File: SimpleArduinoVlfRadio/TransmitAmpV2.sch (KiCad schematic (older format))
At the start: 6 parts

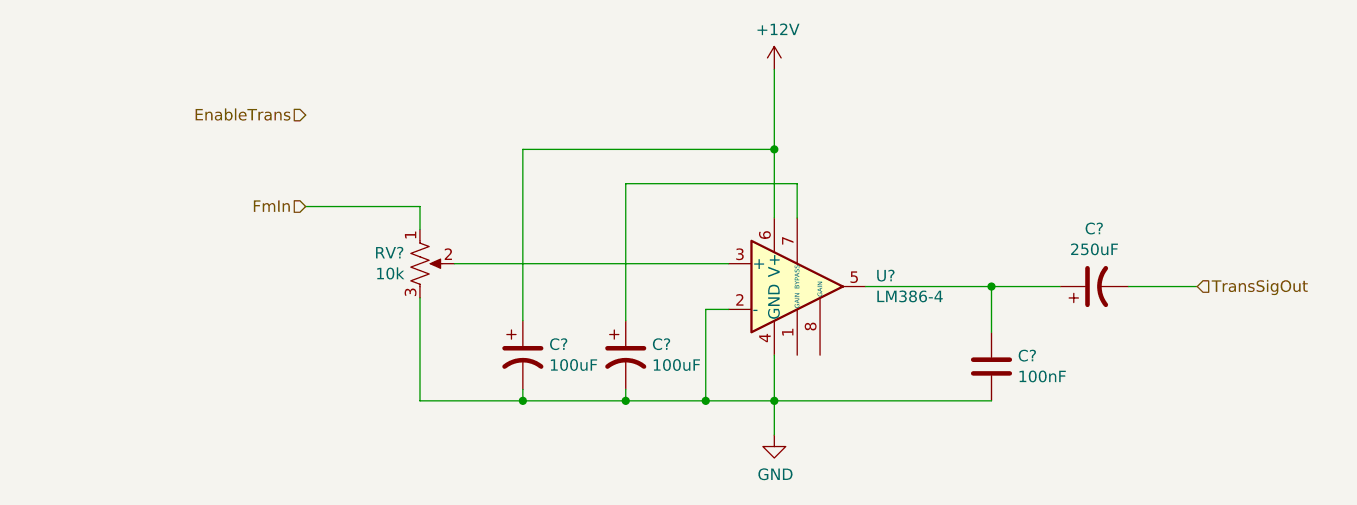
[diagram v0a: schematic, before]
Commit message: Updates to include new transmit amplifier design
Using LM386N-4 instead of LM1875
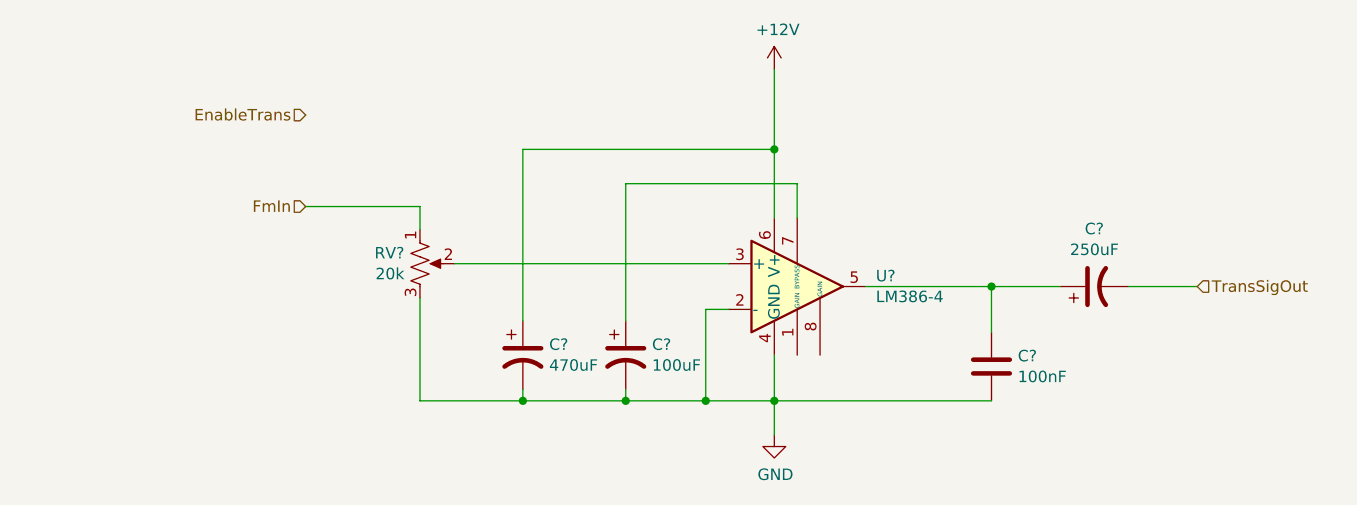
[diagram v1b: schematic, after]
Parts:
- C?: value 100uF -> 470uF
- RV?: value 10k -> 20k
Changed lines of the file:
@@
 P 4600 3750
 F 0 "C?" H 4715 3796 50  0000 L CNN
-F 1 "100uF" H 4715 3705 50  0000 L CNN
+F 1 "470uF" H 4715 3705 50  0000 L CNN
 F 2 "" H 4600 3750 50  0001 C CNN
 F 3 "~" H 4600 3750 50  0001 C CNN
@@
 P 4150 3350
 F 0 "RV?" H 4082 3396 50  0000 R CNN
-F 1 "10k" H 4082 3305 50  0000 R CNN
+F 1 "20k" H 4082 3305 50  0000 R CNN
 F 2 "" H 4150 3350 50  0001 C CNN
 F 3 "~" H 4150 3350 50  0001 C CNN

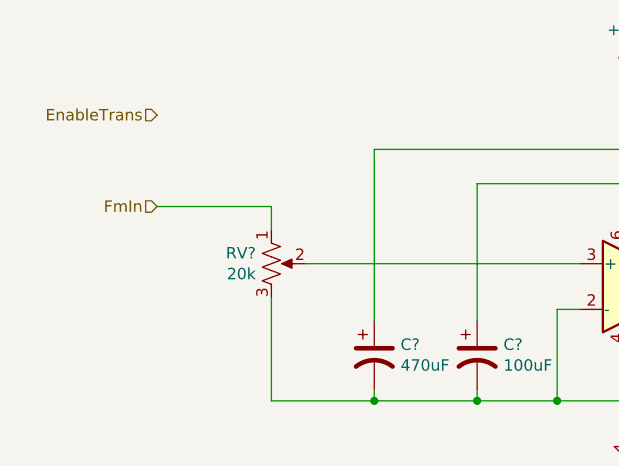
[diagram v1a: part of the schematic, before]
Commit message: Add input capacitor
Filter out DC with an input capacitor.
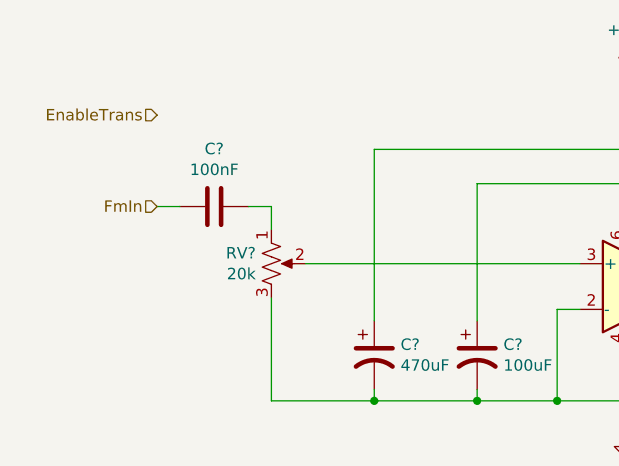
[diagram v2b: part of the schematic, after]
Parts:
- added C?: 100nF, symbol Device:C
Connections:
- net FmIn: now also C?.2; no longer RV?.1
- new net: C?.1, RV?.1
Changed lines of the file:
@@
 Wire Wire Line
 	4150 3200 4150 3100
-Wire Wire Line
-	4150 3100 3650 3100
 Text HLabel 3650 3100 0    50   Input ~ 0
 FmIn
@@
 	5700 2500 5700 2850
 Connection ~ 5700 2850
+$Comp
+L Device:C C?
+U 1 1 61E018D6
+P 3900 3100
+F 0 "C?" V 3648 3100 50  0000 C CNN
+F 1 "100nF" V 3739 3100 50  0000 C CNN
+F 2 "" H 3938 2950 50  0001 C CNN
+F 3 "~" H 3900 3100 50  0001 C CNN
+	1    3900 3100
+	0    1    1    0
+$EndComp
+Wire Wire Line
+	4150 3100 4050 3100
+Wire Wire Line
+	3750 3100 3650 3100
 $EndSCHEMATC

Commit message: Updates to overall layout.
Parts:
- added R?: 100k, symbol Device:R_US
- C?: value 250uF -> 250uF (50V+)
- C?: value 100nF -> 100nF (100V+ Metalized)
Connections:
- net at RV?.1: now also R?.1; no longer C?.1
- new net: C?.1, R?.2
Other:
- moved on the sheet: C?
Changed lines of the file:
@@
 $Descr A4 11693 8268
 encoding utf-8
-Sheet 5 5
+Sheet 4 10
 Title ""
 Date ""
@@
 P 6650 3800
 F 0 "C?" H 6765 3846 50  0000 L CNN
-F 1 "100nF" H 6765 3755 50  0000 L CNN
+F 1 "100nF (100V+ Metalized)" H 6765 3755 50  0000 L CNN
 F 2 "" H 6688 3650 50  0001 C CNN
 F 3 "~" H 6650 3800 50  0001 C CNN
@@
 P 7100 3450
 F 0 "C?" V 7352 3450 50  0000 C CNN
-F 1 "250uF" V 7261 3450 50  0000 C CNN
+F 1 "250uF (50V+)" V 7261 3450 50  0000 C CNN
 F 2 "" H 7100 3450 50  0001 C CNN
 F 3 "~" H 7100 3450 50  0001 C CNN
@@
 	4150 3950 4600 3950
 Connection ~ 4600 3950
-Wire Wire Line
-	4150 3200 4150 3100
-Text HLabel 3650 3100 0    50   Input ~ 0
+Text HLabel 3000 3100 0    50   Input ~ 0
 FmIn
 Text HLabel 7550 3450 2    50   Input ~ 0
 TransSigOut
-Text HLabel 3650 2700 0    50   Input ~ 0
+Text HLabel 3000 2700 0    50   Input ~ 0
 EnableTrans
 Wire Wire Line
@@
 L Device:C C?
 U 1 1 61E018D6
-P 3900 3100
-F 0 "C?" V 3648 3100 50  0000 C CNN
-F 1 "100nF" V 3739 3100 50  0000 C CNN
-F 2 "" H 3938 2950 50  0001 C CNN
-F 3 "~" H 3900 3100 50  0001 C CNN
-	1    3900 3100
+P 3250 3100
+F 0 "C?" V 2998 3100 50  0000 C CNN
+F 1 "100nF" V 3089 3100 50  0000 C CNN
+F 2 "" H 3288 2950 50  0001 C CNN
+F 3 "~" H 3250 3100 50  0001 C CNN
+	1    3250 3100
 	0    1    1    0
 $EndComp
 Wire Wire Line
-	4150 3100 4050 3100
+	3100 3100 3000 3100
+$Comp
+L Device:R_US R?
+U 1 1 61E4A5DB
+P 3750 3100
+F 0 "R?" V 3545 3100 50  0000 C CNN
+F 1 "100k" V 3636 3100 50  0000 C CNN
+F 2 "" V 3790 3090 50  0001 C CNN
+F 3 "~" H 3750 3100 50  0001 C CNN
+	1    3750 3100
+	0    1    1    0
+$EndComp
 Wire Wire Line
-	3750 3100 3650 3100
+	3400 3100 3600 3100
+Wire Wire Line
+	3900 3100 4150 3100
+Wire Wire Line
+	4150 3100 4150 3200
 $EndSCHEMATC

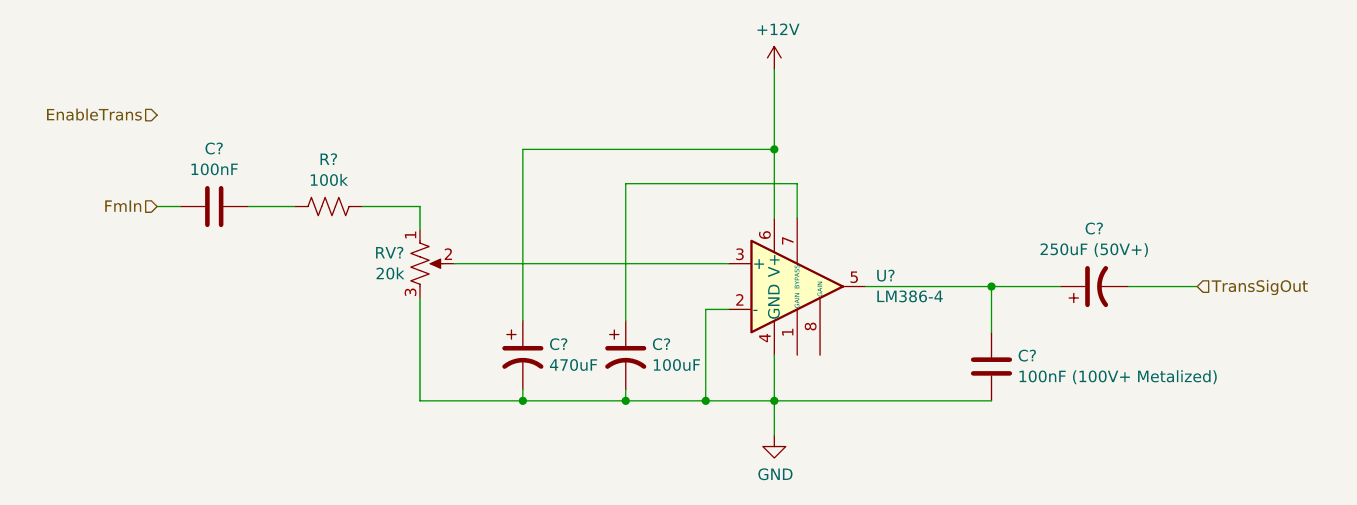
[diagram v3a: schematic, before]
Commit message: Updated Transmitter and finished fsk receiver
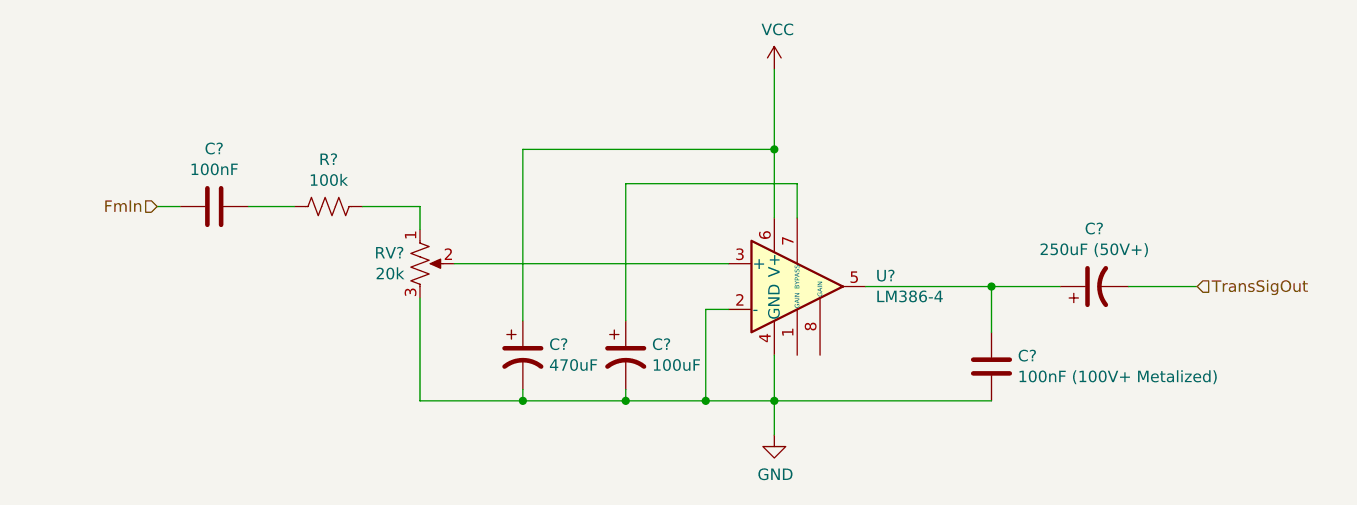
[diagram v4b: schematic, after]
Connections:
- net +12V renamed VCC
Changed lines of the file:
@@
 $Descr A4 11693 8268
 encoding utf-8
-Sheet 4 10
+Sheet 4 14
 Title ""
 Date ""
@@
 $EndDescr
 $Comp
+L power:GND #PWR?
+U 1 1 61DDF91B
+P 5700 4100
+AR Path="/61DDCE18/61DDF91B" Ref="#PWR?"  Part="1"
+AR Path="/62C5E0F5/61DDF91B" Ref="#PWR?"  Part="1"
+F 0 "#PWR?" H 5700 3850 50  0001 C CNN
+F 1 "GND" H 5705 3927 50  0000 C CNN
+F 2 "" H 5700 4100 50  0001 C CNN
+F 3 "" H 5700 4100 50  0001 C CNN
+	1    5700 4100
+	1    0    0    -1
+$EndComp
+Wire Wire Line
+	5500 3550 5400 3550
+Wire Wire Line
+	5400 3550 5400 3950
+Wire Wire Line
+	5400 3950 5700 3950
+Wire Wire Line
+	5700 3950 5700 4100
+Wire Wire Line
+	5700 3750 5700 3950
+Connection ~ 5700 3950
+Wire Wire Line
+	6100 3450 6650 3450
+Wire Wire Line
+	5800 3150 5800 3000
+Wire Wire Line
+	5050 3900 5050 3950
+Wire Wire Line
+	5050 3950 5400 3950
+Connection ~ 5400 3950
+$Comp
+L Device:C C?
+U 1 1 61DE66BC
+P 6650 3800
+AR Path="/61DDCE18/61DE66BC" Ref="C?"  Part="1"
+AR Path="/62C5E0F5/61DE66BC" Ref="C?"  Part="1"
+F 0 "C?" H 6765 3846 50  0000 L CNN
+F 1 "100nF (100V+ Metalized)" H 6765 3755 50  0000 L CNN
+F 2 "" H 6688 3650 50  0001 C CNN
+F 3 "~" H 6650 3800 50  0001 C CNN
+	1    6650 3800
+	1    0    0    -1
+$EndComp
+Wire Wire Line
+	6650 3650 6650 3450
+Connection ~ 6650 3450
+Wire Wire Line
+	6650 3450 6950 3450
+Wire Wire Line
+	6650 3950 5700 3950
+$Comp
+L Device:CP1 C?
+U 1 1 61DE1BB3
+P 5050 3750
+AR Path="/61DDCE18/61DE1BB3" Ref="C?"  Part="1"
+AR Path="/62C5E0F5/61DE1BB3" Ref="C?"  Part="1"
+F 0 "C?" H 5165 3796 50  0000 L CNN
+F 1 "100uF" H 5165 3705 50  0000 L CNN
+F 2 "" H 5050 3750 50  0001 C CNN
+F 3 "~" H 5050 3750 50  0001 C CNN
+	1    5050 3750
+	1    0    0    -1
+$EndComp
+$Comp
+L Device:CP1 C?
+U 1 1 61DE52DF
+P 7100 3450
+AR Path="/61DDCE18/61DE52DF" Ref="C?"  Part="1"
+AR Path="/62C5E0F5/61DE52DF" Ref="C?"  Part="1"
+F 0 "C?" V 7352 3450 50  0000 C CNN
+F 1 "250uF (50V+)" V 7261 3450 50  0000 C CNN
+F 2 "" H 7100 3450 50  0001 C CNN
+F 3 "~" H 7100 3450 50  0001 C CNN
+	1    7100 3450
+	0    -1   -1   0
+$EndComp
+Wire Wire Line
+	5050 3000 5050 3600
+Wire Wire Line
+	5800 3000 5050 3000
+Wire Wire Line
+	7250 3450 7550 3450
+$Comp
+L Device:CP1 C?
+U 1 1 61DE875C
+P 4600 3750
+AR Path="/61DDCE18/61DE875C" Ref="C?"  Part="1"
+AR Path="/62C5E0F5/61DE875C" Ref="C?"  Part="1"
+F 0 "C?" H 4715 3796 50  0000 L CNN
+F 1 "470uF" H 4715 3705 50  0000 L CNN
+F 2 "" H 4600 3750 50  0001 C CNN
+F 3 "~" H 4600 3750 50  0001 C CNN
+	1    4600 3750
+	1    0    0    -1
+$EndComp
+Wire Wire Line
+	4300 3350 5500 3350
+Wire Wire Line
+	5700 2850 4600 2850
+Wire Wire Line
+	4600 2850 4600 3600
+Wire Wire Line
+	5700 2850 5700 3150
+Wire Wire Line
+	4600 3900 4600 3950
+Wire Wire Line
+	4600 3950 5050 3950
+Connection ~ 5050 3950
+$Comp
+L Device:R_POT_US RV?
+U 1 1 61DEA1A6
+P 4150 3350
+AR Path="/61DDCE18/61DEA1A6" Ref="RV?"  Part="1"
+AR Path="/62C5E0F5/61DEA1A6" Ref="RV?"  Part="1"
+F 0 "RV?" H 4082 3396 50  0000 R CNN
+F 1 "20k" H 4082 3305 50  0000 R CNN
+F 2 "" H 4150 3350 50  0001 C CNN
+F 3 "~" H 4150 3350 50  0001 C CNN
+	1    4150 3350
+	1    0    0    -1
+$EndComp
+Wire Wire Line
+	4150 3500 4150 3950
+Wire Wire Line
+	4150 3950 4600 3950
+Connection ~ 4600 3950
+Text HLabel 3000 3100 0    50   Input ~ 0
+FmIn
+Text HLabel 7550 3450 2    50   Input ~ 0
+TransSigOut
+Wire Wire Line
+	5700 2500 5700 2850
+Connection ~ 5700 2850
+$Comp
+L Device:C C?
+U 1 1 61E018D6
+P 3250 3100
+AR Path="/61DDCE18/61E018D6" Ref="C?"  Part="1"
+AR Path="/62C5E0F5/61E018D6" Ref="C?"  Part="1"
+F 0 "C?" V 2998 3100 50  0000 C CNN
+F 1 "100nF" V 3089 3100 50  0000 C CNN
+F 2 "" H 3288 2950 50  0001 C CNN
+F 3 "~" H 3250 3100 50  0001 C CNN
+	1    3250 3100
+	0    1    1    0
+$EndComp
+Wire Wire Line
+	3100 3100 3000 3100
+$Comp
+L Device:R_US R?
+U 1 1 61E4A5DB
+P 3750 3100
+AR Path="/61DDCE18/61E4A5DB" Ref="R?"  Part="1"
+AR Path="/62C5E0F5/61E4A5DB" Ref="R?"  Part="1"
+F 0 "R?" V 3545 3100 50  0000 C CNN
+F 1 "100k" V 3636 3100 50  0000 C CNN
+F 2 "" V 3790 3090 50  0001 C CNN
+F 3 "~" H 3750 3100 50  0001 C CNN
+	1    3750 3100
+	0    1    1    0
+$EndComp
+Wire Wire Line
+	3400 3100 3600 3100
+Wire Wire Line
+	3900 3100 4150 3100
+Wire Wire Line
+	4150 3100 4150 3200
+$Comp
 L Amplifier_Audio:LM386 U?
 U 1 1 61DDD0F9
@@
 $EndComp
 $Comp
-L power:+12V #PWR?
-U 1 1 61DDF214
+L power:VCC #PWR?
+U 1 1 62C7F6CA
 P 5700 2500
 F 0 "#PWR?" H 5700 2350 50  0001 C CNN
-F 1 "+12V" H 5715 2673 50  0000 C CNN
+F 1 "VCC" H 5715 2673 50  0000 C CNN
 F 2 "" H 5700 2500 50  0001 C CNN
 F 3 "" H 5700 2500 50  0001 C CNN
@@
 	1    0    0    -1
 $EndComp
-$Comp
-L power:GND #PWR?
-U 1 1 61DDF91B
-P 5700 4100
-F 0 "#PWR?" H 5700 3850 50  0001 C CNN
-F 1 "GND" H 5705 3927 50  0000 C CNN
-F 2 "" H 5700 4100 50  0001 C CNN
-F 3 "" H 5700 4100 50  0001 C CNN
-	1    5700 4100
-	1    0    0    -1
-$EndComp
-Wire Wire Line
-	5500 3550 5400 3550
-Wire Wire Line
-	5400 3550 5400 3950
-Wire Wire Line
-	5400 3950 5700 3950
-Wire Wire Line
-	5700 3950 5700 4100
-Wire Wire Line
-	5700 3750 5700 3950
-Connection ~ 5700 3950
-Wire Wire Line
-	6100 3450 6650 3450
-Wire Wire Line
-	5800 3150 5800 3000
-Wire Wire Line
-	5050 3900 5050 3950
-Wire Wire Line
-	5050 3950 5400 3950
-Connection ~ 5400 3950
-$Comp
-L Device:C C?
-U 1 1 61DE66BC
-P 6650 3800
-F 0 "C?" H 6765 3846 50  0000 L CNN
-F 1 "100nF (100V+ Metalized)" H 6765 3755 50  0000 L CNN
-F 2 "" H 6688 3650 50  0001 C CNN
-F 3 "~" H 6650 3800 50  0001 C CNN
-	1    6650 3800
-	1    0    0    -1
-$EndComp
-Wire Wire Line
-	6650 3650 6650 3450
-Connection ~ 6650 3450
-Wire Wire Line
-	6650 3450 6950 3450
-Wire Wire Line
-	6650 3950 5700 3950
-$Comp
-L Device:CP1 C?
-U 1 1 61DE1BB3
-P 5050 3750
-F 0 "C?" H 5165 3796 50  0000 L CNN
-F 1 "100uF" H 5165 3705 50  0000 L CNN
-F 2 "" H 5050 3750 50  0001 C CNN
-F 3 "~" H 5050 3750 50  0001 C CNN
-	1    5050 3750
-	1    0    0    -1
-$EndComp
-$Comp
-L Device:CP1 C?
-U 1 1 61DE52DF
-P 7100 3450
-F 0 "C?" V 7352 3450 50  0000 C CNN
-F 1 "250uF (50V+)" V 7261 3450 50  0000 C CNN
-F 2 "" H 7100 3450 50  0001 C CNN
-F 3 "~" H 7100 3450 50  0001 C CNN
-	1    7100 3450
-	0    -1   -1   0
-$EndComp
-Wire Wire Line
-	5050 3000 5050 3600
-Wire Wire Line
-	5800 3000 5050 3000
-Wire Wire Line
-	7250 3450 7550 3450
-$Comp
-L Device:CP1 C?
-U 1 1 61DE875C
-P 4600 3750
-F 0 "C?" H 4715 3796 50  0000 L CNN
-F 1 "470uF" H 4715 3705 50  0000 L CNN
-F 2 "" H 4600 3750 50  0001 C CNN
-F 3 "~" H 4600 3750 50  0001 C CNN
-	1    4600 3750
-	1    0    0    -1
-$EndComp
-Wire Wire Line
-	4300 3350 5500 3350
-Wire Wire Line
-	5700 2850 4600 2850
-Wire Wire Line
-	4600 2850 4600 3600
-Wire Wire Line
-	5700 2850 5700 3150
-Wire Wire Line
-	4600 3900 4600 3950
-Wire Wire Line
-	4600 3950 5050 3950
-Connection ~ 5050 3950
-$Comp
-L Device:R_POT_US RV?
-U 1 1 61DEA1A6
-P 4150 3350
-F 0 "RV?" H 4082 3396 50  0000 R CNN
-F 1 "20k" H 4082 3305 50  0000 R CNN
-F 2 "" H 4150 3350 50  0001 C CNN
-F 3 "~" H 4150 3350 50  0001 C CNN
-	1    4150 3350
-	1    0    0    -1
-$EndComp
-Wire Wire Line
-	4150 3500 4150 3950
-Wire Wire Line
-	4150 3950 4600 3950
-Connection ~ 4600 3950
-Text HLabel 3000 3100 0    50   Input ~ 0
-FmIn
-Text HLabel 7550 3450 2    50   Input ~ 0
-TransSigOut
-Text HLabel 3000 2700 0    50   Input ~ 0
-EnableTrans
-Wire Wire Line
-	5700 2500 5700 2850
-Connection ~ 5700 2850
-$Comp
-L Device:C C?
-U 1 1 61E018D6
-P 3250 3100
-F 0 "C?" V 2998 3100 50  0000 C CNN
-F 1 "100nF" V 3089 3100 50  0000 C CNN
-F 2 "" H 3288 2950 50  0001 C CNN
-F 3 "~" H 3250 3100 50  0001 C CNN
-	1    3250 3100
-	0    1    1    0
-$EndComp
-Wire Wire Line
-	3100 3100 3000 3100
-$Comp
-L Device:R_US R?
-U 1 1 61E4A5DB
-P 3750 3100
-F 0 "R?" V 3545 3100 50  0000 C CNN
-F 1 "100k" V 3636 3100 50  0000 C CNN
-F 2 "" V 3790 3090 50  0001 C CNN
-F 3 "~" H 3750 3100 50  0001 C CNN
-	1    3750 3100
-	0    1    1    0
-$EndComp
-Wire Wire Line
-	3400 3100 3600 3100
-Wire Wire Line
-	3900 3100 4150 3100
-Wire Wire Line
-	4150 3100 4150 3200
 $EndSCHEMATC
